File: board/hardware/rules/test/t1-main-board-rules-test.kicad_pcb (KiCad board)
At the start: 6 copper layers, 80 x 478.9 mm, 69 parts, among them U1 test, U2 test, U3 test, U4 test, U5 test, U6 test

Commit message: Rules: PCB-I-09 leaves a footprint's own pads out
The master-clock spacing fired between the CS43198's MCLK pin and its
neighbours and between the dividers' pins: the maker's pin pitch, not a
routing choice. The rule now skips pad pairs of one footprint, as PCB-V-01
does; a test row checks two footprints (fires) against one (does not).
The test board script finds kicad-lib's tools in libs' kicad/ folder.
Main board DRC: the six PCB-I-09 warnings are gone, 0 errors.

Co-Authored-By: Claude Opus 5.5 <noreply@anthropic.com>
Claude-Session: https://claude.ai/code/session_01Ei262h3TpgY9vyfNLMi5Mn
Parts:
- removed the R10 at (56.5, 266.1)
- removed the R13 at (56.9, 286.9)
- removed the R19 at (45.5, 296.4)
- added R11: test, , F.Cu at (40.3, 295.2)
- added R16: test, , F.Cu at (55.5, 300.2)
- added R22: test, , F.Cu at (41.5, 309.2)
- added R26: test, , F.Cu at (41.5, 473.2)
- added R27: test, , F.Cu at (55.5, 473.2)
- added U7: test, , F.Cu at (55.0, 214.3)
- moved U5 267.8 mm to (55.1, 188.6)
- moved U6 242.3 mm to (41.0, 214.3)
- moved U3 54.1 mm to (54.0, 153.4)
- moved U2 30.5 mm to (40.6, 153.4)
- moved U1 26.9 mm to (40.0, 153.4)
- moved U4 22.2 mm to (41.1, 188.6)
- moved R10 20.5 mm to (56.5, 274.4)
- moved TP5 8.30 mm to (40.0, 257.4)
- moved TP6 8.30 mm to (54.0, 257.4)
- moved C1 8.30 mm to (45.5, 183.4)
- moved C2 8.30 mm to (59.5, 183.4)
- moved C3 8.30 mm to (40.5, 206.4)
- moved D1 8.30 mm to (43.5, 481.7)
- moved D2 8.30 mm to (54.5, 481.7)
- moved H10 8.30 mm to (55.1, 183.4)
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- renumbered R11 to R10, R16 to R13, R22 to R19, R26 to U8, R27 to U9
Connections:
- FID1 pad 1: N37 -> N39
- FID2 pad 1: N39 -> N41
- H5 pad 1: N30 -> N32
- R10 pad 1: N51 -> N50
- R12 pad 1: N52 -> N54
- R14 pad 1: N54 -> N56
- R15 pad 1: N54 -> N56
- R17 pad 1: N55 -> N57
- R19 pad 1: N56 -> DDR_50SE_1
- R23 pad 1: N56 -> N58
- R24 pad 1: N57 -> N59
- R25 pad 1: N57 -> N59
- R9 pad 1: N47 -> N49
- TP1 pad 1: N35 -> N37
- TP10 pad 1: N46 -> N48
- TP11 pad 1: N47 -> N49
- TP12 pad 1: N48 -> N50
- TP13 pad 1: N49 -> N51
- TP14 pad 1: N50 -> N52
- TP2 pad 1: N36 -> N38
- TP3 pad 1: N41 -> N43
- TP4 pad 1: N42 -> N44
- TP5 pad 1: N43 -> N45
- TP6 pad 1: N44 -> N46
- TP7 pad 1: N45 -> N47
- TP8 pad 1: N45 -> N47
- TP9 pad 1: N46 -> N48
- U1 pad 1: N31 -> MCLK_50SE_3
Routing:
- net N31: track 0.00 -> 4.20 mm
- net N30: track 0.00 -> 4.20 mm
- net N29: track 4.20 -> 0.00 mm
- net N28: track 4.20 -> 0.00 mm
- net N66: track 0.00 -> 3.00 mm
- net N61: track 3.00 -> 0.00 mm, vias 0 -> 1
- net N60: track 3.00 -> 0.00 mm, vias 0 -> 1
- net N36: track 0.00 -> 3.00 mm
- net N35: track 0.00 -> 3.00 mm
- net N34: track 3.00 -> 0.00 mm
- net N33: track 3.00 -> 0.00 mm
- net MCLK_50SE_9: track 0.00 -> 3.00 mm
- net MCLK_50SE_8: track 0.00 -> 3.00 mm
- net MCLK_50SE_3: track 2.90 -> 0.00 mm
- net MCLK_50SE_4: track 2.90 -> 0.00 mm
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- added copper zone on F.Cu, net N58
- added copper zone on F.Cu, net N59
- removed copper zone on F.Cu, net N54
- removed copper zone on F.Cu, net N55
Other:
- board size 80 x 478.9 mm -> 80 x 487.2 mm

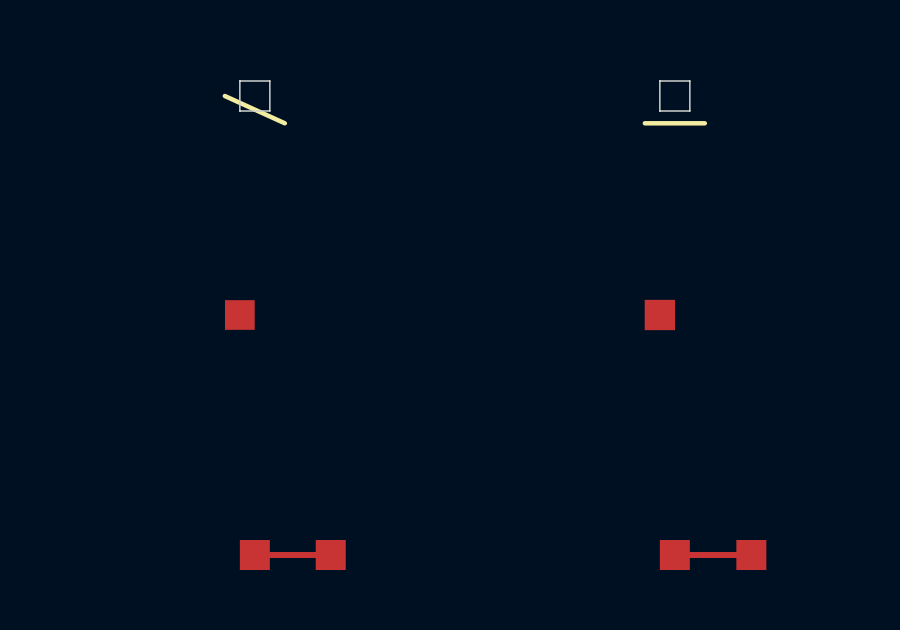
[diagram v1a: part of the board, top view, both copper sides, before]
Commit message: Compaction: lower inductors, 0201 decoupling, 0.8 mm signal test pads
A matrix tool (hardware/studies/compaction) checks each candidate against
the design's stresses: same inductance, design peak <= 70 % and the
converter's maximum limit <= 100 % of Isat (30 % drop), height zones,
ratings at least twice the rail, PCB-D-06; sourcing outcome per part.

Applied (placement v1 decision 12, BOM v1.15):
- L601, L4401: XGL4015-102MEC (1.5 mm) for XAL/XGL4020-102MEC (2.1 mm);
- L1001, L5101: XGL4015-471MEC (1.5 mm) for Wurth 744373240047, on the
  stock XxL4020 land (the Wurth land was never drawn);
- L1201 is 1.2 mm (XGL4012, per-MPN heights): it moves next to the SoC;
- 58 x 100 nF decoupling on rails <= 3.3 V in core/IO/radio: 0201;
- 51 test pads on signal nets: 0.8 mm (PCB-D-06 v0.16, JLCPCB guide).
Kept: L901, L2802 (XGL4015 at 103 % of Isat at the limit); no thinner
0805/1206 capacitor passes (obsolete, NRND or unlisted).

Board need 113 % -> 111 % (core band 227 -> 203 %, power band 258 ->
233 %, radio band 19 -> 0 %); only C904 still relies on PCB-Z-04.
ERC 0 errors, craft Q1 met, DRC 0 errors (605 warnings), pcb and study
tests pass, rules test board PASS.

Co-Authored-By: Claude Opus 5.5 <noreply@anthropic.com>
Claude-Session: https://claude.ai/code/session_01Ei262h3TpgY9vyfNLMi5Mn
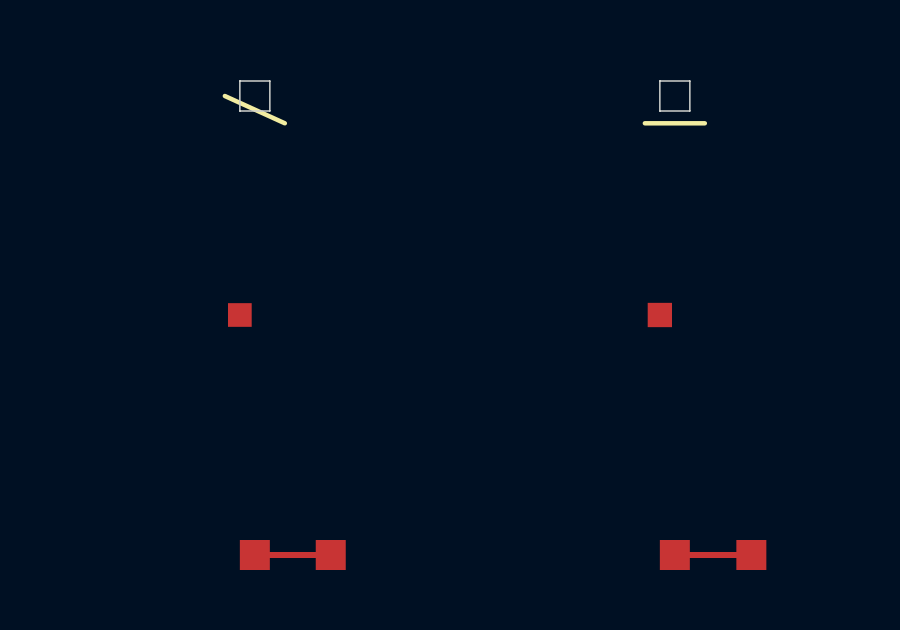
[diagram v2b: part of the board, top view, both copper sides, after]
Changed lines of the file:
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@@
 		(pad "1" smd rect
 			(at 0 0)
-			(size 1.01 1.01)
+			(size 0.81 0.81)
 			(property pad_prop_testpoint)
 			(layers "F.Cu" "F.Mask" "F.Paste")
@@
 		(pad "1" smd rect
 			(at 0 0)
-			(size 0.99 0.99)
+			(size 0.79 0.79)
 			(property pad_prop_testpoint)
 			(layers "F.Cu" "F.Mask" "F.Paste")

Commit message: Board: hole-to-inner-copper at the fab's six-layer row (PCB-G-11)
Every drill, via and hole rule checked against the fab's six-layer rows:
only the hole-to-inner-conductor clearance depends on the layer count
(8 mil for six layers; the composed fab rules carried the eight-layer
9 mil). New product override PCB-G-11 with its test row (check_drc
PASS, 87/87); the laser-drill basis noted as layer-independent. Rules
recomposed; main board DRC 0 errors.

Co-Authored-By: Claude Opus 5.5 <noreply@anthropic.com>
Claude-Session: https://claude.ai/code/session_013P6pW9LdyEMFishwCcZGUr
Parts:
- added H13: test, , F.Cu at (41.1, 192.1)
- added H14: test, , F.Cu at (55.1, 192.1)
- moved H1 129.2 mm to (40.2, 32.5)
- moved H2 129.2 mm to (54.2, 32.5)
- moved H8 3.94 mm to (55.4, 176.0)
- moved H7 3.92 mm to (41.4, 176.0)
- moved C1 3.50 mm to (45.5, 186.9)
- moved C2 3.50 mm to (59.5, 186.9)
- moved C3 3.50 mm to (40.5, 209.9)
- moved C4 3.50 mm to (54.5, 209.9)
- moved C5 3.50 mm to (44.2, 217.8)
- moved C6 3.50 mm to (58.3, 217.8)
- moved D1 3.50 mm to (43.5, 485.2)
- moved D2 3.50 mm to (54.5, 485.2)
- moved FID1 3.50 mm to (40.5, 232.8)
- moved FID2 3.50 mm to (54.5, 232.8)
- moved R1 3.50 mm to (40.3, 36.0)
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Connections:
- FID1 pad 1: N39 -> N41
- FID2 pad 1: N41 -> N43
- R1 pad 1: N19 -> N21
- R10 pad 1: N50 -> N52
- R11 pad 1: N53 -> N55
- R12 pad 1: N54 -> N56
- R13 pad 1: N55 -> N57
- R14 pad 1: N56 -> N58
- R15 pad 1: N56 -> N58
- R16 pad 1: N57 -> N59
- R17 pad 1: N57 -> N59
- R2 pad 1: N21 -> N23
- R22 pad 1: N58 -> N60
- R23 pad 1: N58 -> N60
- R24 pad 1: N59 -> N61
- R25 pad 1: N59 -> N61
- R26 pad 1: N68 -> N70
- R9 pad 1: N49 -> N51
- TP1 pad 1: N37 -> N39
- TP10 pad 1: N48 -> N50
- TP11 pad 1: N49 -> N51
- TP12 pad 1: N50 -> N52
- TP13 pad 1: N51 -> N53
- TP14 pad 1: N52 -> N54
- TP2 pad 1: N38 -> N40
- TP3 pad 1: N43 -> N45
- TP4 pad 1: N44 -> N46
- TP5 pad 1: N45 -> N47
- TP6 pad 1: N46 -> N48
- TP7 pad 1: N47 -> N49
- TP8 pad 1: N47 -> N49
- TP9 pad 1: N48 -> N50
- U2 pad 2: N28 -> N30
- U3 pad 2: N29 -> N31
- U4 pad 1: N33 -> N35
- U5 pad 1: N34 -> N36
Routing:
- net N33: track 0.00 -> 4.20 mm
- net N32: track 0.00 -> 4.20 mm
- net N31: track 4.20 -> 0.00 mm
- net N30: track 4.20 -> 0.00 mm
- net N68: track 0.00 -> 3.00 mm
- net N63: track 3.00 -> 0.00 mm, vias 0 -> 1
- net N62: track 3.00 -> 0.00 mm, vias 0 -> 1
- net N38: track 0.00 -> 3.00 mm
- net N37: track 0.00 -> 3.00 mm
- net N36: track 3.00 -> 0.00 mm
- net N35: track 3.00 -> 0.00 mm
- net N29: track 0.00 -> 3.00 mm
- net N28: track 0.00 -> 3.00 mm
- net N67: track 0.19 -> 3.00 mm
- net N48: track 2.55 -> 0.00 mm
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- added copper zone on F.Cu, net N60
- added copper zone on F.Cu, net N61
- removed copper zone on F.Cu, net N56
- removed copper zone on F.Cu, net N57
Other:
- board size 80 x 487.2 mm -> 80 x 490.7 mm
- board text added: "T1 PCB-G-11 [Q1]: Hole to copper, inner layers (six-layer row)"
